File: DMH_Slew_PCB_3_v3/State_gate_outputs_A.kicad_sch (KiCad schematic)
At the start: 25 parts, among them J4 TS_Jack_6.35mm_Sw, J5 TS_Jack_6.35mm_Sw, Q5 BC548, Q6 BC548, U1 TL074

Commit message: PCB 3 comp placement done
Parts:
- Q5, Q6: footprint Package_TO_SOT_THT:TO-92_Inline -> Package_TO_SOT_THT:TO-92L_Inline_Wide
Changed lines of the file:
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@@
 			)
 		)
-		(property "Footprint" "Package_TO_SOT_THT:TO-92_Inline"
+		(property "Footprint" "Package_TO_SOT_THT:TO-92L_Inline_Wide"
 			(at 252.73 36.195 0)
 			(effects
@@
 			)
 		)
-		(property "Footprint" "Package_TO_SOT_THT:TO-92_Inline"
+		(property "Footprint" "Package_TO_SOT_THT:TO-92L_Inline_Wide"
 			(at 252.73 103.505 0)
 			(effects

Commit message: Adjustments after prototyping
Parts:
- R37: value 1k8 -> 2k2
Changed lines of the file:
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@@
 			)
 		)
-		(property "Value" "1k8"
+		(property "Value" "2k2"
 			(at 252.73 46.9899 0)
 			(effects

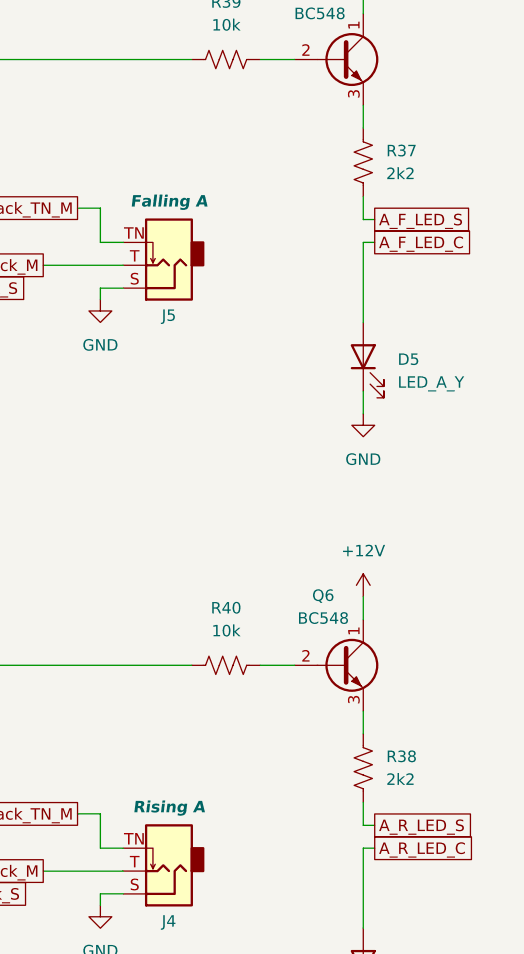
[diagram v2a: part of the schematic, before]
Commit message: Corrected PCB 2 switch positions
and Regenerated Gerbers
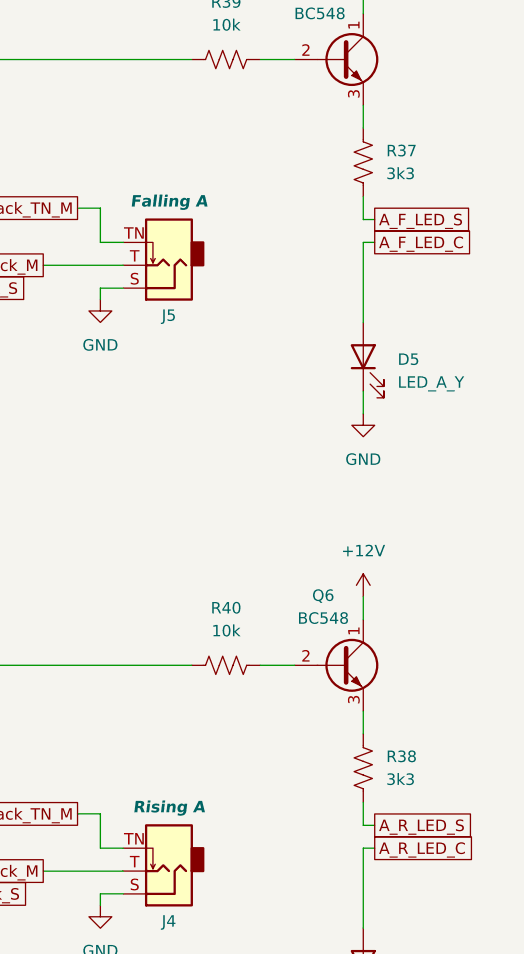
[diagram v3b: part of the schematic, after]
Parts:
- R37, R38: value 2k2 -> 3k3
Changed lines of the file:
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@@
 			)
 		)
-		(property "Value" "2k2"
+		(property "Value" "3k3"
 			(at 252.73 114.2999 0)
 			(effects
@@
 			)
 		)
-		(property "Value" "2k2"
+		(property "Value" "3k3"
 			(at 252.73 46.9899 0)
 			(effects

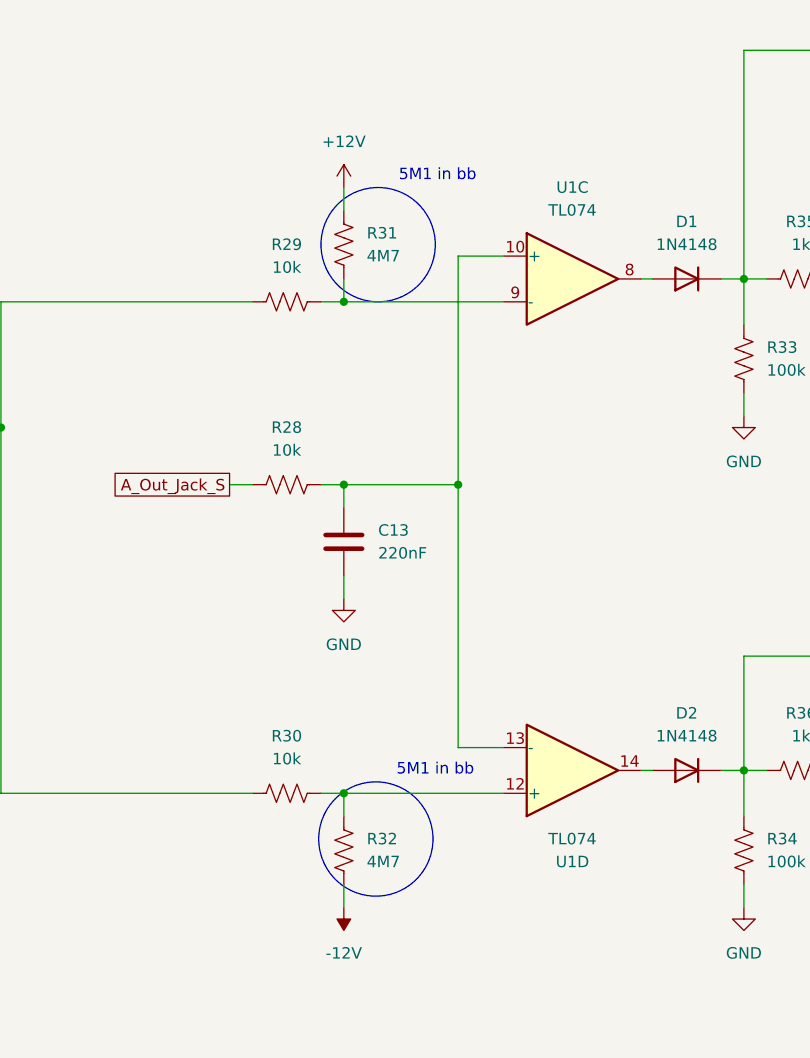
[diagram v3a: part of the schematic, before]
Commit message: Redesigned Main PCB
and regenerated Gerbers
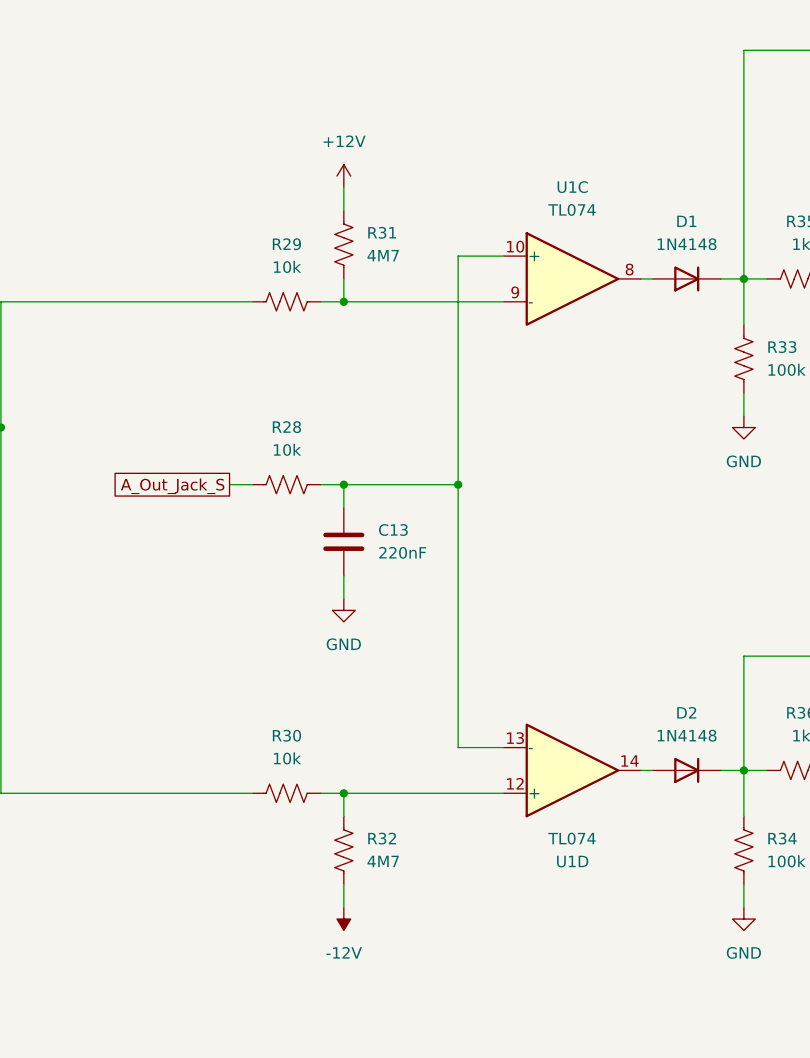
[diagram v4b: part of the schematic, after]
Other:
- note removed: "5M1 in bb"
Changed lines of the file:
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@@
 		(comment 1 "PCB for 5 cm Kosmo format synthesizer module")
-	)
-	(circle
-		(center 130.81 55.88)
-		(radius 6.35)
-		(stroke
-			(width 0)
-			(type default)
-		)
-		(fill
-			(type none)
-		)
-	)
-	(circle
-		(center 130.556 121.92)
-		(radius 6.35)
-		(stroke
-			(width 0)
-			(type default)
-		)
-		(fill
-			(type none)
-		)
-	)
-	(text "5M1 in bb"
-		(exclude_from_sim no)
-		(at 137.16 114.3 0)
-		(effects
-			(font
-				(size 1.27 1.27)
-			)
-		)
-	)
-	(text "5M1 in bb"
-		(exclude_from_sim no)
-		(at 137.414 48.26 0)
-		(effects
-			(font
-				(size 1.27 1.27)
-			)
-		)
 	)
 	(junction
